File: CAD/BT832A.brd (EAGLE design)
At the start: 24.9 x 50 mm, 43 parts, among them IC1 CP2102, U1 MCP73831T-3ACI/OT, U2 BT832, U3 LP5907MFX-3.3/NOPB, U4 LP5907MFX-3.3/NOPB, U5 ADS131M08IPBS, U6 BCM857BS, X1 ABM3B-8.000MHZ-B2-T, X2 FC-12M

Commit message: Update BT832A.brd
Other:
- board size 24.9 x 50 mm -> 24.9 x 49.9 mm
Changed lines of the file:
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@@
 ADC inputs may have to be a (CHEAP) SMT connector backside to minimize possible interference from the radio,
 but let's just break them out first and test. Let's still ID a 16-20 pin connector.</text>
-<wire x1="6.604" y1="-27.94" x2="6.604" y2="19.558" width="0.1524" layer="20"/>
+<wire x1="6.604" y1="-27.813" x2="6.604" y2="19.558" width="0.1524" layer="20"/>
 <wire x1="6.604" y1="19.558" x2="7.874" y2="20.828" width="0.1524" layer="20" curve="-90"/>
 <wire x1="7.874" y1="20.828" x2="30.226" y2="20.828" width="0.1524" layer="20"/>
 <wire x1="30.226" y1="20.828" x2="31.496" y2="19.558" width="0.1524" layer="20" curve="-90"/>
 <wire x1="31.496" y1="19.558" x2="31.496" y2="-27.94" width="0.1524" layer="20"/>
-<wire x1="31.496" y1="-27.94" x2="30.226" y2="-29.21" width="0.1524" layer="20" curve="-90"/>
-<wire x1="30.226" y1="-29.21" x2="7.874" y2="-29.21" width="0.1524" layer="20"/>
-<wire x1="7.874" y1="-29.21" x2="6.604" y2="-27.94" width="0.1524" layer="20" curve="-90"/>
-<dimension x1="38.862" y1="20.828" x2="31.75" y2="-29.21" x3="36.83" y3="-4.191" textsize="1.778" layer="47" dtype="vertical"/>
+<wire x1="31.496" y1="-27.94" x2="30.226" y2="-29.083" width="0.1524" layer="20" curve="-90"/>
+<wire x1="30.226" y1="-29.083" x2="7.874" y2="-29.083" width="0.1524" layer="20"/>
+<wire x1="7.874" y1="-29.083" x2="6.604" y2="-27.813" width="0.1524" layer="20" curve="-90"/>
 <dimension x1="6.604" y1="19.558" x2="31.496" y2="18.796" x3="19.05" y3="23.114" textsize="1.778" layer="47" dtype="horizontal"/>
 <hole x="30.2006" y="19.6088" drill="1.5"/>
 <hole x="7.8232" y="19.6596" drill="1.5"/>
-<hole x="30.1752" y="-27.813" drill="1.5"/>
-<hole x="16.7386" y="-27.7876" drill="1.5"/>
+<hole x="30.1752" y="-27.686" drill="1.5"/>
+<hole x="16.7386" y="-27.6606" drill="1.5"/>
 <hole x="30.1752" y="-20.1168" drill="1.5"/>
 <text x="11.2014" y="-13.3096" size="0.6096" layer="21" rot="R180">S1</text>
@@
  JACOB TINKHAUSER
       MIT LICENSE</text>
+<dimension x1="31.496" y1="-29.083" x2="29.464" y2="20.828" x3="34.5186" y3="-4.1275" textsize="1.778" layer="47" dtype="vertical"/>
 </plain>
 <attributes>
@@
 <vertex x="6.604" y="-7.9756"/>
 <vertex x="31.496" y="-7.9756"/>
-<vertex x="31.496" y="-29.21"/>
-<vertex x="6.604" y="-29.21"/>
+<vertex x="31.496" y="-29.083"/>
+<vertex x="6.604" y="-29.083"/>
 </polygon>
 <polygon width="0.1524" layer="16">
@@
 </polygon>
 <polygon width="0.1524" layer="1">
-<vertex x="6.604" y="-29.21"/>
+<vertex x="6.604" y="-29.083"/>
 <vertex x="6.604" y="-7.9756"/>
 <vertex x="28.6512" y="-7.9756"/>
@@
 <vertex x="6.604" y="13.0556"/>
 <vertex x="31.496" y="13.0556"/>
-<vertex x="31.496" y="-29.21"/>
+<vertex x="31.496" y="-29.083"/>
 </polygon>
 <via x="27.6352" y="4.2926" extent="1-16" drill="0.35"/>
@@
 <via x="8.0264" y="-18.415" extent="1-16" drill="0.35"/>
 <via x="9.0932" y="-24.0792" extent="1-16" drill="0.35"/>
-<via x="13.6144" y="-27.7114" extent="1-16" drill="0.35"/>
+<via x="13.6144" y="-27.5844" extent="1-16" drill="0.35"/>
 <via x="17.7038" y="-24.6126" extent="1-16" drill="0.35"/>
 <via x="27.813" y="-22.8854" extent="1-16" drill="0.35"/>
@@
 <contactref element="C14" pad="1"/>
 <contactref element="C15" pad="1"/>
-<via x="18.9484" y="-27.7622" extent="1-16" drill="0.35"/>
+<via x="18.9484" y="-27.6352" extent="1-16" drill="0.35"/>
 <contactref element="U$1" pad="MP1"/>
 <contactref element="U$1" pad="MP2"/>
@@
 <wire x1="9.0932" y1="-24.0792" x2="13.3604" y2="-14.4376" width="0" layer="19" extent="1-1"/>
 <wire x1="14.2156" y1="-25.1554" x2="9.0932" y2="-24.0792" width="0" layer="19" extent="1-1"/>
-<wire x1="13.6144" y1="-27.7114" x2="14.2156" y2="-25.1554" width="0" layer="19" extent="1-1"/>
+<wire x1="13.6144" y1="-27.5844" x2="14.2156" y2="-25.1554" width="0" layer="19" extent="1-1"/>
 <wire x1="17.7038" y1="-24.6126" x2="14.2156" y2="-25.1554" width="0" layer="19" extent="1-1"/>
 <wire x1="20.0406" y1="-22.7584" x2="17.7038" y2="-24.6126" width="0" layer="19" extent="1-1"/>
@@
 <wire x1="26.288" y1="-27.5914" x2="25.938" y2="-24.9164" width="0" layer="19" extent="1-1"/>
 <wire x1="22.988" y1="-27.5914" x2="26.288" y2="-27.5914" width="0" layer="19" extent="1-1"/>
-<wire x1="18.9484" y1="-27.7622" x2="17.7038" y2="-24.6126" width="0" layer="19" extent="1-1"/>
+<wire x1="18.9484" y1="-27.6352" x2="17.7038" y2="-24.6126" width="0" layer="19" extent="1-1"/>
 <wire x1="19.1008" y1="-10.3274" x2="19.9644" y2="-14.2136" width="0" layer="19" extent="1-16"/>
 <wire x1="17.4094" y1="-9.906" x2="19.1008" y2="-10.3274" width="0" layer="19" extent="16-16"/>

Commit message: edits
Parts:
- added C17: 4.7uF, adafruit:C0402
- moved R6 0.43 mm to (21.3, -14.0)
- moved R5 0.41 mm to (19.9, -14.0)
- moved R1 0.05 mm to (17.3, -18.2)
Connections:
- net GND: now also C17.1
- net NVD: now also C17.2
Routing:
- net N$14: track 11.3 -> 10.6 mm
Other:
- board text added: "TOP"

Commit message: Update BT832A.brd
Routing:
- net GND: track 26.2 -> 40.9 mm, vias 28 -> 32

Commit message: more edits
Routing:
- net GND: track 40.9 -> 43.1 mm, vias 32 -> 33
- net D+: track 11.8 -> 12.6 mm
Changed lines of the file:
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@@
 <attribute name="MF" value="Texas Instruments" x="21.2344" y="28.194" size="1.778" layer="28" rot="MR0" display="off"/>
 <attribute name="MP" value="LP5907MFX-3.3/NOPB" x="21.2344" y="28.194" size="1.778" layer="28" rot="MR0" display="off"/>
-<attribute name="NAME" x="17.286359375" y="-7.9914" size="0.4023875" layer="26" rot="MR0"/>
+<attribute name="NAME" x="16.549759375" y="-9.0582" size="0.4023875" layer="26" rot="MR0"/>
 <attribute name="PACKAGE" value="SOT-23 Texas Instruments" x="21.2344" y="28.194" size="1.778" layer="28" rot="MR0" display="off"/>
 <attribute name="PRICE" value="None" x="21.2344" y="28.194" size="1.778" layer="28" rot="MR0" display="off"/>
@@
 <via x="30.0228" y="-25.0698" extent="1-16" drill="0.35"/>
 <via x="18.1356" y="-12.573" extent="1-16" drill="0.35"/>
-<via x="10.5156" y="-25.5778" extent="1-16" drill="0.35"/>
+<via x="10.5156" y="-25.4508" extent="1-16" drill="0.35"/>
 <via x="24.5618" y="4.6482" extent="1-16" drill="0.35"/>
 <wire x1="27.5844" y1="-0.2032" x2="28.1203375" y2="-0.7391375" width="0.3048" layer="16"/>
@@
 <wire x1="23.5966" y1="-8.3312" x2="30.1244" y2="-8.3312" width="0.3048" layer="16"/>
 <via x="30.1498" y="-5.207" extent="1-16" drill="0.35"/>
-<wire x1="25.0501" y1="-13.5439" x2="24.8526" y2="-15.1464" width="0" layer="19" extent="1-1"/>
+<wire x1="24.8526" y1="-15.1464" x2="24.1634" y2="-15.1464" width="0.1524" layer="1"/>
+<wire x1="24.1634" y1="-15.1464" x2="23.0886" y2="-14.0716" width="0.1524" layer="1"/>
+<via x="10.4648" y="-22.7584" extent="1-16" drill="0.35"/>
+<wire x1="25.6898" y1="-8.382" x2="30.1498" y2="-5.207" width="0" layer="19" extent="1-1"/>
 <wire x1="28.8544" y1="-11.2164" x2="25.6898" y2="-8.382" width="0" layer="19" extent="1-1"/>
-<wire x1="30.1498" y1="-5.207" x2="25.6898" y2="-8.382" width="0" layer="19" extent="1-1"/>
 </signal>
 <signal name="XTAL2_2">
@@
 <wire x1="25.0952" y1="-23.5204" x2="24.638" y2="-23.9776" width="0.254" layer="1"/>
 <via x="25.1206" y="-23.1902" extent="1-16" drill="0.35"/>
-<via x="23.8506" y="-15.0622" extent="1-16" drill="0.35"/>
-<wire x1="24.324" y1="-16.1106125" x2="23.8506" y2="-15.6372125" width="0.254" layer="16"/>
-<wire x1="23.8506" y1="-15.0622" x2="23.8506" y2="-15.6372125" width="0.254" layer="16"/>
+<via x="23.2156" y="-15.24" extent="1-16" drill="0.35"/>
+<wire x1="24.324" y1="-16.1106125" x2="23.4533875" y2="-15.24" width="0.254" layer="16"/>
+<wire x1="23.2156" y1="-15.24" x2="23.4533875" y2="-15.24" width="0.254" layer="16"/>
 <wire x1="25.1206" y1="-22.9108" x2="25.1206" y2="-23.1902" width="0.254" layer="16"/>
 <wire x1="25.1206" y1="-22.9108" x2="24.324" y2="-22.1142" width="0.254" layer="16"/>
 <wire x1="24.324" y1="-22.1142" x2="24.324" y2="-16.1106125" width="0.254" layer="16"/>
-<wire x1="24.8526" y1="-15.6464" x2="24.4348" y2="-15.6464" width="0.254" layer="1"/>
-<wire x1="24.4348" y1="-15.6464" x2="23.8506" y2="-15.0622" width="0.254" layer="1"/>
+<wire x1="24.8526" y1="-15.6464" x2="23.622" y2="-15.6464" width="0.254" layer="1"/>
+<wire x1="23.622" y1="-15.6464" x2="23.2156" y2="-15.24" width="0.254" layer="1"/>
 </signal>
 <signal name="ID">

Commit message: edit
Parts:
- moved S1 0.87 mm to (9.96, -14.7)
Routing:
- net B+: track 10.00 -> 10.6 mm
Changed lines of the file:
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@@
 <attribute name="VALUE" x="21.7424" y="-15.7226" size="0.381" layer="27" rot="R180"/>
 </element>
-<element name="S1" library="CL-SB-12B-01T" package="CL-SB-12B" value="CL-SB-12B-01T" x="10.7696" y="-15.0114" smashed="yes" rot="R90">
-<attribute name="AVAILABILITY" value="In Stock" x="10.7696" y="-15.0114" size="1.778" layer="27" rot="R90" display="off"/>
-<attribute name="DESCRIPTION" value=" Slide Switch SPDT Surface Mount " x="10.7696" y="-15.0114" size="1.778" layer="27" rot="R90" display="off"/>
-<attribute name="MF" value="Nidec Copal" x="10.7696" y="-15.0114" size="1.778" layer="27" rot="R90" display="off"/>
-<attribute name="MP" value="CL-SB-12B-01T" x="10.7696" y="-15.0114" size="1.778" layer="27" rot="R90" display="off"/>
-<attribute name="PACKAGE" value="None" x="10.7696" y="-15.0114" size="1.778" layer="27" rot="R90" display="off"/>
-<attribute name="PRICE" value="None" x="10.7696" y="-15.0114" size="1.778" layer="27" rot="R90" display="off"/>
+<element name="S1" library="CL-SB-12B-01T" package="CL-SB-12B" value="CL-SB-12B-01T" x="9.9568" y="-14.7066" smashed="yes" rot="R90">
+<attribute name="AVAILABILITY" value="In Stock" x="9.9568" y="-14.7066" size="1.778" layer="27" rot="R90" display="off"/>
+<attribute name="DESCRIPTION" value=" Slide Switch SPDT Surface Mount " x="9.9568" y="-14.7066" size="1.778" layer="27" rot="R90" display="off"/>
+<attribute name="MF" value="Nidec Copal" x="9.9568" y="-14.7066" size="1.778" layer="27" rot="R90" display="off"/>
+<attribute name="MP" value="CL-SB-12B-01T" x="9.9568" y="-14.7066" size="1.778" layer="27" rot="R90" display="off"/>
+<attribute name="PACKAGE" value="None" x="9.9568" y="-14.7066" size="1.778" layer="27" rot="R90" display="off"/>
+<attribute name="PRICE" value="None" x="9.9568" y="-14.7066" size="1.778" layer="27" rot="R90" display="off"/>
 </element>
 <element name="JP1" library="adafruit" library_urn="urn:adsk.eagle:library:420" package="1X08-CLEANBIG" package3d_urn="urn:adsk.eagle:package:6240708/1" value="" x="30.226" y="8.6614" smashed="yes" rot="R270">
@@
 <element name="C16" library="adafruit" library_urn="urn:adsk.eagle:library:420" package="C0402" package3d_urn="urn:adsk.eagle:package:6240340/1" value="4.7uF" x="13.3604" y="-15.0876" smashed="yes" rot="R270">
 <attribute name="NAME" x="12.6238" y="-13.8684" size="0.508" layer="25"/>
-<attribute name="VALUE" x="12.3698" y="-15.7988" size="0.508" layer="27" rot="R90"/>
+<attribute name="VALUE" x="12.4968" y="-15.9258" size="0.508" layer="27" rot="R90"/>
 </element>
 <element name="C17" library="adafruit" library_urn="urn:adsk.eagle:library:420" package="C0402" package3d_urn="urn:adsk.eagle:package:6240340/1" value="4.7uF" x="20.447" y="-11.811" smashed="yes" rot="R180">
@@
 <contactref element="U$1" pad="MP1"/>
 <contactref element="U$1" pad="MP2"/>
-<via x="10.7696" y="-15.0622" extent="1-16" drill="0.35"/>
+<via x="10.0076" y="-14.8336" extent="1-16" drill="0.35"/>
 <via x="30.734" y="-18.415" extent="1-16" drill="0.35"/>
 <contactref element="C16" pad="1"/>
@@
 <contactref element="S1" pad="1"/>
 <contactref element="J1" pad="2"/>
-<wire x1="14.2156" y1="-23.1554" x2="13.0196" y2="-21.53204375" width="0.508" layer="1"/>
-<wire x1="13.0196" y1="-17.5114" x2="13.0196" y2="-21.53204375" width="0.508" layer="1"/>
+<wire x1="14.2156" y1="-23.1554" x2="12.2068" y2="-20.4288125" width="0.508" layer="1"/>
+<wire x1="12.2068" y1="-17.2066" x2="12.2068" y2="-20.4288125" width="0.508" layer="1"/>
 <contactref element="U1" pad="3"/>
-<wire x1="13.0196" y1="-17.5114" x2="13.0196" y2="-16.1142" width="0.508" layer="1"/>
+<wire x1="12.2068" y1="-17.2066" x2="12.2068" y2="-16.927" width="0.508" layer="1"/>
 <wire x1="15.2908" y1="-15.494" x2="13.6398" y2="-15.494" width="0.508" layer="1"/>
 <wire x1="13.6398" y1="-15.494" x2="13.3604" y2="-15.7734" width="0.508" layer="1"/>
 <contactref element="C16" pad="2"/>
-<wire x1="13.3604" y1="-15.7734" x2="13.0196" y2="-16.1142" width="0.508" layer="1"/>
+<wire x1="13.3604" y1="-15.7734" x2="12.2068" y2="-16.927" width="0.508" layer="1"/>
 <wire x1="13.3604" y1="-15.7376" x2="13.3604" y2="-15.7734" width="0.1524" layer="1"/>
 </signal>
@@
 <contactref element="D3" pad="3"/>
 <contactref element="S1" pad="3"/>
-<wire x1="13.553" y1="-11.978" x2="13.553" y2="-9.5426" width="0.508" layer="1"/>
-<wire x1="13.0196" y1="-12.5114" x2="13.553" y2="-11.978" width="0.508" layer="1"/>
+<wire x1="13.553" y1="-10.8604" x2="13.553" y2="-9.5426" width="0.508" layer="1"/>
+<wire x1="12.2068" y1="-12.2066" x2="13.553" y2="-10.8604" width="0.508" layer="1"/>
 <wire x1="13.553" y1="-9.5426" x2="16.129" y2="-9.5426" width="0.508" layer="1"/>
 </signal>

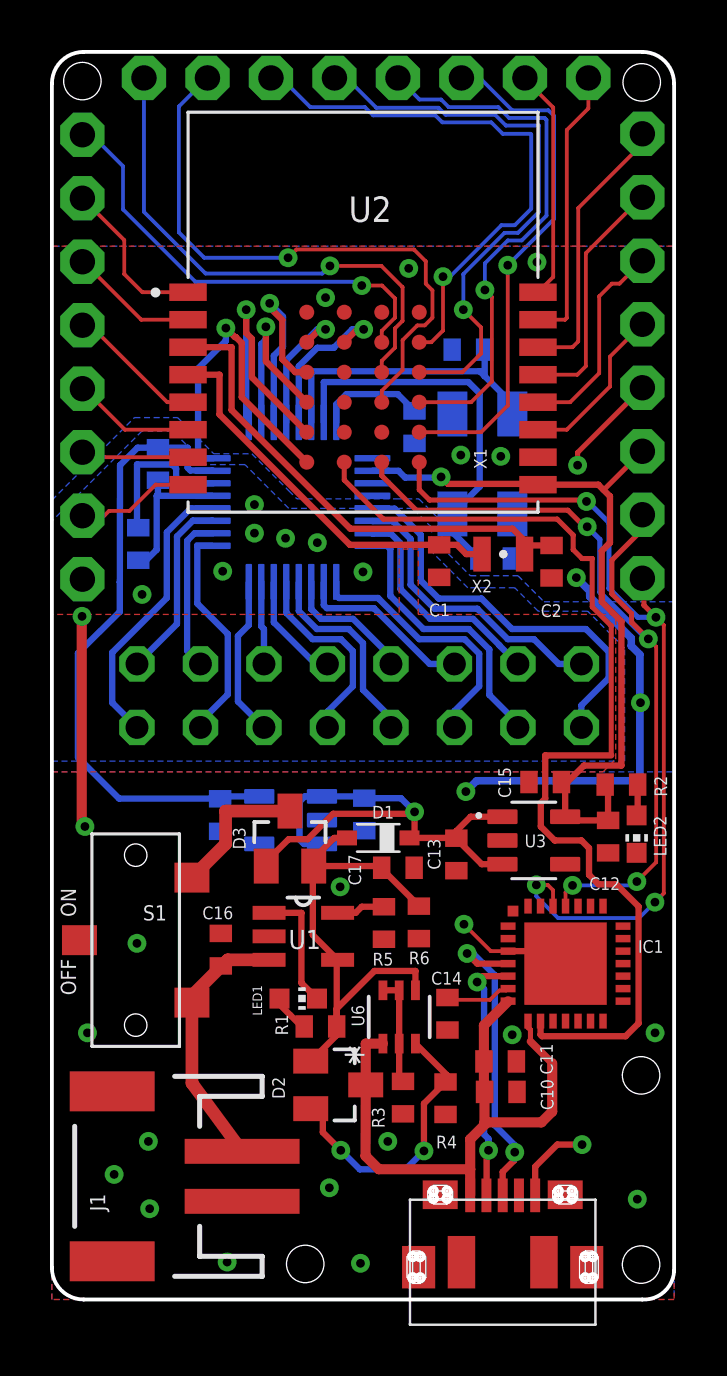
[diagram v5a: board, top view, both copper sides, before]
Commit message: replace with 20 pin cp2102
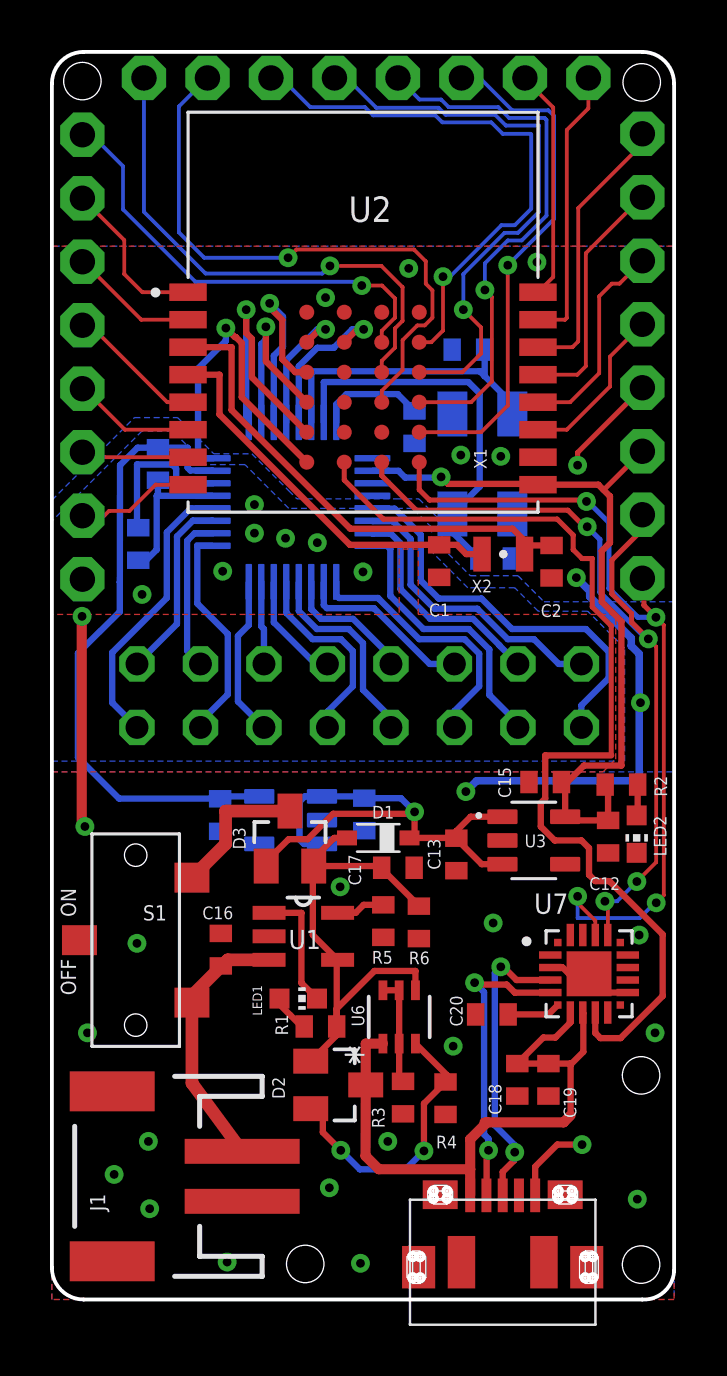
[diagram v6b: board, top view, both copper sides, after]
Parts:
- removed C10: 1.0uF, adafruit:C0402
- removed C11, C14: 0.1uF, adafruit:C0402
- removed IC1: CP2102, silabs:MLP28
- added C18: 1.0uF, adafruit:C0402
- added C19, C20: 0.1uF, adafruit:C0402
- added U7: CP2102N-A02-GQFN20R, CP2102N-A02-GQFN20R:SILABS_CP2102N-A02-GQFN20R
- moved R5 0.08 mm to (19.9, -13.9)
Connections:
- net +5V: now also C18.2, C19.2, U7.7, U7.8; no longer C10.2, C11.2, IC1.7, IC1.8
- net CPRST: now also U7.9; no longer IC1.9
- net CPVDD: now also C20.2, U7.6; no longer C14.2, IC1.6
- net D+: now also U7.4; no longer IC1.4
- net D-: now also U7.5; no longer IC1.5
- net GND: now also C18.1, C19.1, C20.1, U7.12, U7.21, U7.3; no longer C10.1, C11.1, C14.1, IC1.3, IC1.EXP, IC1.M
- net RXD: now also U7.17; no longer IC1.25
- net TXD: now also U7.18; no longer IC1.26
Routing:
- net D-: track 10.1 -> 12.0 mm
- net GND: track 43.1 -> 41.8 mm, vias 33 -> 34
- net CPRST: track 41.4 -> 40.2 mm
- net TXD: track 34.9 -> 33.8 mm
- net +5V: track 25.0 -> 26.1 mm
- net D+: track 12.6 -> 12.0 mm
- net CPVDD: track 2.65 -> 2.14 mm
- net RXD: track 35.0 -> 34.5 mm
